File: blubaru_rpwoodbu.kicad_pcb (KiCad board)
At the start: 2 copper layers, 97.8 x 94.6 mm, 38 parts, among them J1 DB15, J2 DB15, J3 FSA2269, J4 ProMicro, J5 RN52_BREAKOUT, J6 JACK_TRS_6PINS, J7 TPA6112, P1 CONN_01X06, U1 DG419

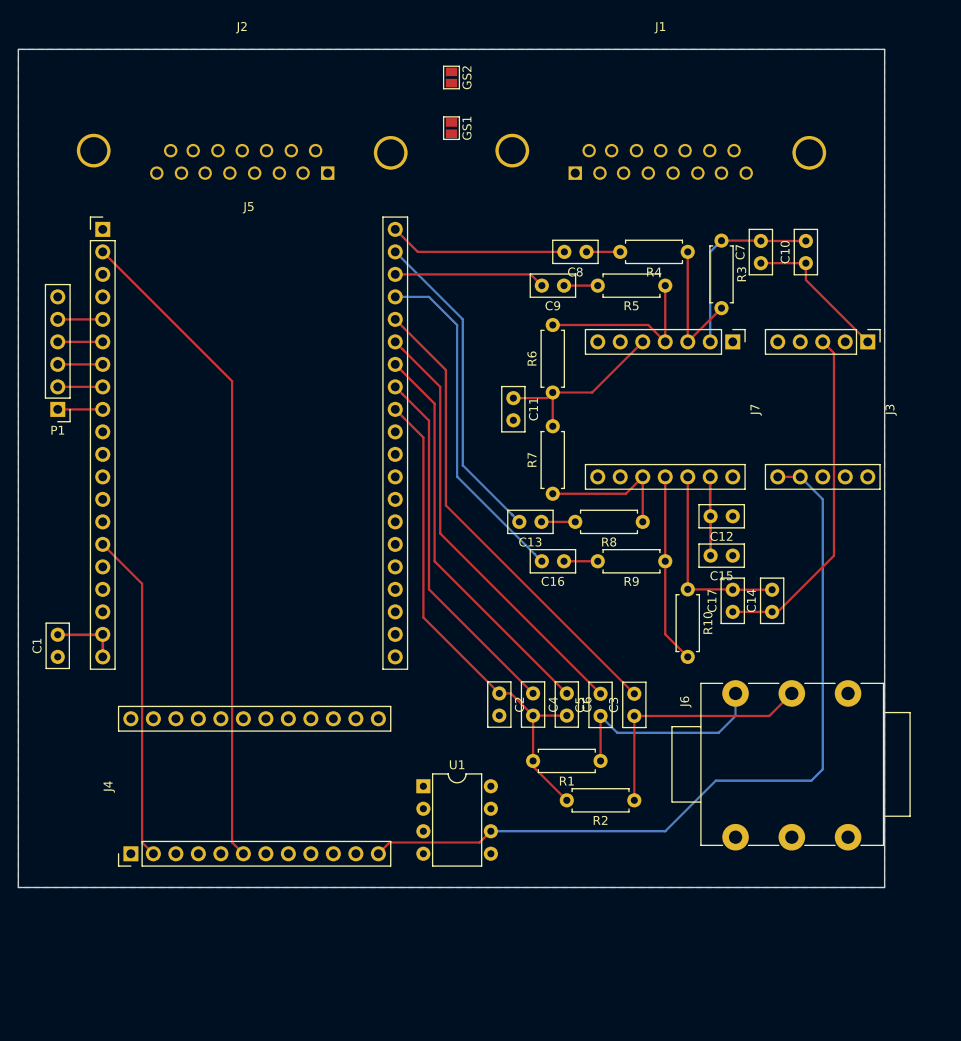
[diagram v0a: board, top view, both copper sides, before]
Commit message: jbebels attempt at routing
All power and audio is routed, as is the crystal and UART lines. Other
digital lines remain, and the resistors for the LEDs are moved off-board
until I figure out the best place for them.

This also required a small fix to the schematic. A junction was missing,
causing the audio grounds to not be connected to the cd/stereo audio
ground.
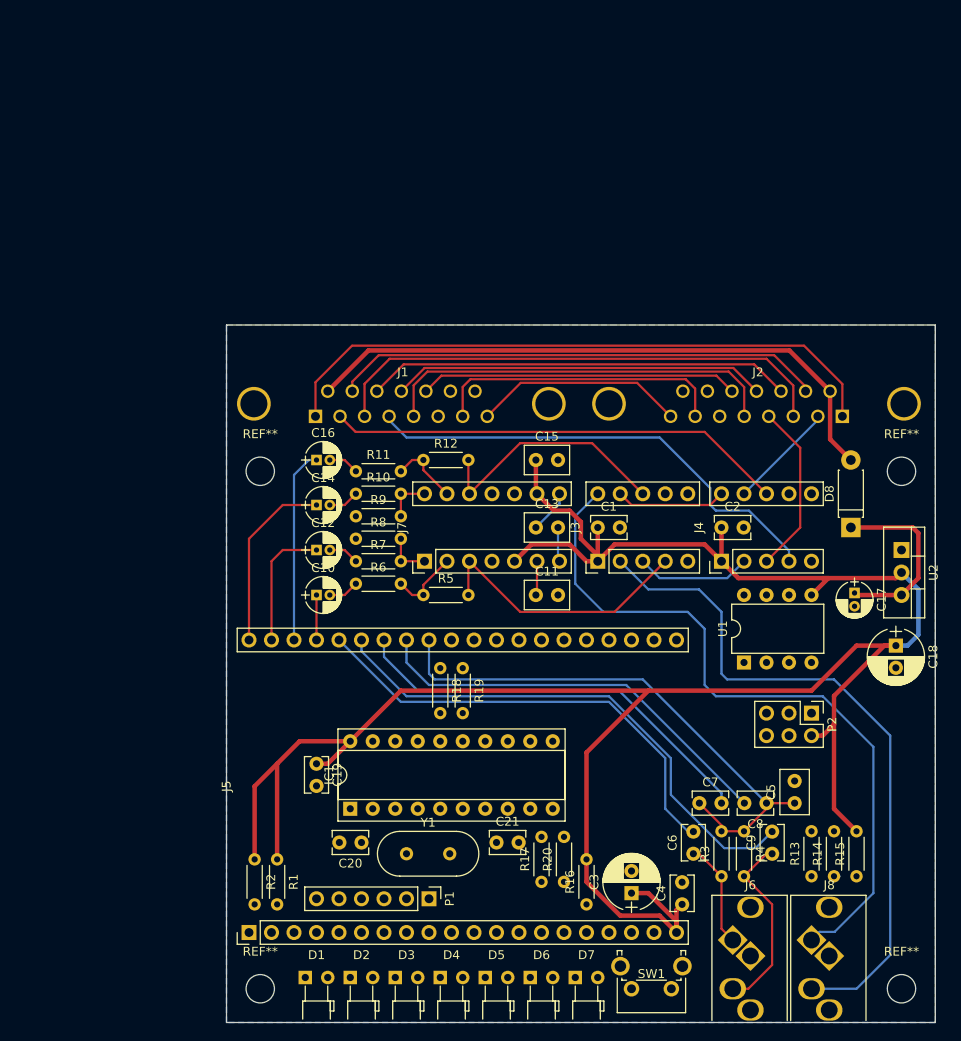
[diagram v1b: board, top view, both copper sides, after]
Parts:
- removed GS1, GS2: GS2, Connectors:GS2
- added C18: 100uF, blubaru:CP_Radial_D6.3mm_P2.50mm, F.Cu at (183.5, 97.2)
- added C19: 0.1uF, blubaru:C_Disc_D4.0mm_W2.6mm_P2.50mm, F.Cu at (118.1, 110.5)
- added C20: 22pF, blubaru:C_Disc_D4.0mm_W2.6mm_P2.50mm, F.Cu at (123.2, 119.4)
- added C21: 22pF, blubaru:C_Disc_D4.0mm_W2.6mm_P2.50mm, F.Cu at (138.4, 119.4)
- added D1: R LED, blubaru:LED_D3.0mm_Horizontal_O1.27mm_Z6.0mm, F.Cu at (116.8, 134.6)
- added D2: B LED, blubaru:LED_D3.0mm_Horizontal_O1.27mm_Z6.0mm, F.Cu at (121.9, 134.6)
- added D3: Y LED, blubaru:LED_D3.0mm_Horizontal_O1.27mm_Z6.0mm, F.Cu at (127.0, 134.6)
- added D4: O LED, blubaru:LED_D3.0mm_Horizontal_O1.27mm_Z6.0mm, F.Cu at (132.1, 134.6)
- added D5: G LED, blubaru:LED_D3.0mm_Horizontal_O1.27mm_Z6.0mm, F.Cu at (137.2, 134.6)
- added D6: B LED, blubaru:LED_D3.0mm_Horizontal_O1.27mm_Z6.0mm, F.Cu at (142.2, 134.6)
- added D7: R LED, blubaru:LED_D3.0mm_Horizontal_O1.27mm_Z6.0mm, F.Cu at (147.3, 134.6)
- added D8: D, Diodes_THT:D_DO-41_SOD81_P7.62mm_Horizontal, F.Cu at (178.4, 83.8)
- added IC1: ATTINY4313-P, blubaru:DIP-20_W7.62mm_Socket, F.Cu at (121.9, 115.6)
- added J8: JACK_TRS_5PINS, blubaru:sj1-353xng, F.Cu at (176.0, 138.3)
- added P2: CONN_02X03, Pin_Headers:Pin_Header_Straight_2x03_Pitch2.54mm, F.Cu at (174.0, 104.8)
- added R11: 11k, Resistors_THT:R_Axial_DIN0204_L3.6mm_D1.6mm_P5.08mm_Horizontal, F.Cu at (122.6, 77.5)
- added R12: 8.2k, Resistors_THT:R_Axial_DIN0204_L3.6mm_D1.6mm_P5.08mm_Horizontal, F.Cu at (130.2, 76.2)
- added R13: 100k, Resistors_THT:R_Axial_DIN0204_L3.6mm_D1.6mm_P5.08mm_Horizontal, F.Cu at (174.0, 123.2)
- added R14: 100k, Resistors_THT:R_Axial_DIN0204_L3.6mm_D1.6mm_P5.08mm_Horizontal, F.Cu at (176.5, 123.2)
- added R15: 1M, Resistors_THT:R_Axial_DIN0204_L3.6mm_D1.6mm_P5.08mm_Horizontal, F.Cu at (179.1, 123.2)
- added R16: 750, Resistors_THT:R_Axial_DIN0204_L3.6mm_D1.6mm_P5.08mm_Horizontal, F.Cu at (148.6, 126.4)
- added R17: 330, Resistors_THT:R_Axial_DIN0204_L3.6mm_D1.6mm_P5.08mm_Horizontal, F.Cu at (143.5, 123.8)
- added R18: 750, Resistors_THT:R_Axial_DIN0204_L3.6mm_D1.6mm_P5.08mm_Horizontal, F.Cu at (132.1, 99.7)
- added R19: 750, Resistors_THT:R_Axial_DIN0204_L3.6mm_D1.6mm_P5.08mm_Horizontal, F.Cu at (134.6, 99.7)
- added R20: 330, Resistors_THT:R_Axial_DIN0204_L3.6mm_D1.6mm_P5.08mm_Horizontal, F.Cu at (146.1, 123.8)
- added REF**: MountingHole_3.2mm_M3, Mounting_Holes:MountingHole_3.2mm_M3, F.Cu at (184.2, 135.9)
- added REF**: MountingHole_3.2mm_M3, Mounting_Holes:MountingHole_3.2mm_M3, F.Cu at (111.8, 135.9)
- added REF**: MountingHole_3.2mm_M3, Mounting_Holes:MountingHole_3.2mm_M3, F.Cu at (184.2, 77.5)
- added REF**: MountingHole_3.2mm_M3, Mounting_Holes:MountingHole_3.2mm_M3, F.Cu at (111.8, 77.5)
- added SW1: SW_Push, blubaru:SW_Tactile_SPST_Angled_PTS645Vx58-2LFS, F.Cu at (158.2, 135.9)
- added U2: LD1117V33, TO_SOT_Packages_THT:TO-220_Vertical, F.Cu at (184.2, 86.4)
- added Y1: 11.0592MHz, Crystals:Crystal_HC49-4H_Vertical, F.Cu at (128.3, 120.7)
- C1: footprint Capacitors_THT:C_Disc_D5.0mm_W2.5mm_P2.50mm -> blubaru:C_Disc_D4.0mm_W2.6mm_P2.50mm
- C10, C14: value 100uF -> 1uF; footprint Capacitors_THT:C_Disc_D5.0mm_W2.5mm_P2.50mm -> blubaru:CP_Radial_D4.0mm_P1.50mm
- C11, C13: footprint Capacitors_THT:C_Disc_D5.0mm_W2.5mm_P2.50mm -> blubaru:C_Disc_D5.0mm_W3.2mm_P2.50mm
- C12: value 0.1uF -> 1uF; footprint Capacitors_THT:C_Disc_D5.0mm_W2.5mm_P2.50mm -> blubaru:CP_Radial_D4.0mm_P1.50mm
- C15: value 10uF -> 1uF; footprint Capacitors_THT:C_Disc_D5.0mm_W2.5mm_P2.50mm -> blubaru:C_Disc_D5.0mm_W3.2mm_P2.50mm
- C16: footprint Capacitors_THT:C_Disc_D5.0mm_W2.5mm_P2.50mm -> blubaru:CP_Radial_D4.0mm_P1.50mm
- C17: value 100uF -> 10uF; footprint Capacitors_THT:C_Disc_D5.0mm_W2.5mm_P2.50mm -> blubaru:CP_Radial_D4.0mm_P1.50mm
- C2: value 1uF -> 0.1uF; footprint Capacitors_THT:C_Disc_D5.0mm_W2.5mm_P2.50mm -> blubaru:C_Disc_D4.0mm_W2.6mm_P2.50mm
- C3: value 47nF -> 220uF; footprint Capacitors_THT:C_Disc_D5.0mm_W2.5mm_P2.50mm -> blubaru:CP_Radial_D6.3mm_P2.50mm
- C4: value 47nF -> 0.1uF; footprint Capacitors_THT:C_Disc_D5.0mm_W2.5mm_P2.50mm -> blubaru:C_Disc_D4.0mm_W2.6mm_P2.50mm
- C5: value 47nF -> 1uF; footprint Capacitors_THT:C_Disc_D5.0mm_W2.5mm_P2.50mm -> blubaru:C_Disc_D5.0mm_W3.2mm_P2.50mm
- C6: value 47nF -> 0.047uF; footprint Capacitors_THT:C_Disc_D5.0mm_W2.5mm_P2.50mm -> blubaru:C_Disc_D4.0mm_W2.6mm_P2.50mm
- C7: value 100uF -> 0.047uF; footprint Capacitors_THT:C_Disc_D5.0mm_W2.5mm_P2.50mm -> blubaru:C_Disc_D4.0mm_W2.6mm_P2.50mm
- C8, C9: value 1uF -> 0.047uF; footprint Capacitors_THT:C_Disc_D5.0mm_W2.5mm_P2.50mm -> blubaru:C_Disc_D4.0mm_W2.6mm_P2.50mm
- J1: footprint Connectors:DB15FC -> blubaru:DB15FC
- J2: footprint Connectors:DB15MC -> blubaru:DB15MC
- J3: value FSA2269 -> TS5A22364-Q1; footprint blubaru:FSA2269 -> blubaru:TS5A22364-Q1
- J4: value ProMicro -> TS5A22364-Q1; footprint blubaru:ProMicro -> blubaru:TS5A22364-Q1
- J6: value JACK_TRS_6PINS -> JACK_TRS_5PINS; footprint Connectors:NMJ6HCD2 -> blubaru:sj1-353xng
- J7: value TPA6112 -> DRV632; footprint blubaru:TPA6112 -> blubaru:DRV632
- R1: value 2k2 -> 330; footprint Resistors_THT:R_Axial_DIN0207_L6.3mm_D2.5mm_P7.62mm_Horizontal -> Resistors_THT:R_Axial_DIN0204_L3.6mm_D1.6mm_P5.08mm_Horizontal
- R10, R6, R7: value 47k -> 11k; footprint Resistors_THT:R_Axial_DIN0207_L6.3mm_D2.5mm_P7.62mm_Horizontal -> Resistors_THT:R_Axial_DIN0204_L3.6mm_D1.6mm_P5.08mm_Horizontal
- R2: value 2k2 -> 750; footprint Resistors_THT:R_Axial_DIN0207_L6.3mm_D2.5mm_P7.62mm_Horizontal -> Resistors_THT:R_Axial_DIN0204_L3.6mm_D1.6mm_P5.08mm_Horizontal
- R3: value 47k -> 2k2; footprint Resistors_THT:R_Axial_DIN0207_L6.3mm_D2.5mm_P7.62mm_Horizontal -> Resistors_THT:R_Axial_DIN0204_L3.6mm_D1.6mm_P5.08mm_Horizontal
- R4: value 22k -> 2k2; footprint Resistors_THT:R_Axial_DIN0207_L6.3mm_D2.5mm_P7.62mm_Horizontal -> Resistors_THT:R_Axial_DIN0204_L3.6mm_D1.6mm_P5.08mm_Horizontal
- R5, R8, R9: value 22k -> 8.2k; footprint Resistors_THT:R_Axial_DIN0207_L6.3mm_D2.5mm_P7.62mm_Horizontal -> Resistors_THT:R_Axial_DIN0204_L3.6mm_D1.6mm_P5.08mm_Horizontal
- moved J4 72.8 mm to (163.8, 83.8)
- moved R3 71.8 mm to (163.8, 123.2), turned to 90 degrees
- moved P1 69.3 mm to (130.8, 125.7), turned to 270 degrees
- moved C9 68.3 mm to (169.5, 120.7), turned to 90 degrees
- moved C10 66.8 mm to (118.1, 91.4), turned to 0 degrees
- moved R4 65.7 mm to (166.4, 118.1), turned to 270 degrees
- moved C8 65.5 mm to (168.9, 114.9)
- moved J2 64.3 mm to (177.5, 71.3)
- moved J5 62.9 mm to (110.5, 113.0), turned to 90 degrees
- moved C1 62.7 mm to (149.9, 83.8), turned to 0 degrees
- moved C7 61.4 mm to (161.3, 114.9), turned to 0 degrees
- moved C14 52.8 mm to (118.1, 81.3), turned to 0 degrees
- moved C12 47.1 mm to (118.1, 86.4), turned to 0 degrees
- moved R5 44.3 mm to (130.2, 91.4), turned to 0 degrees
- moved R2 43.4 mm to (111.1, 121.3), turned to 270 degrees
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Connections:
- C1 pad 1: GND -> VCC
- C1 pad 2: VCC -> GND
- C10 pad 1: /DB-15 interconnects/Modules/Audio switch/BT_L -> /DB-15 interconnects/Modules/Bluetooth Module/Line Driver/R-
- C12 pad 1: GND -> /DB-15 interconnects/Modules/Bluetooth Module/Line Driver/R+
- C12 pad 2: VCC -> Net-(C12-Pad2)
- C13 pad 2: /DB-15 interconnects/Modules/Bluetooth Module/Amp/R+ -> Net-(C13-Pad2)
- C14 pad 1: /DB-15 interconnects/Modules/Audio switch/BT_R -> /DB-15 interconnects/Modules/Bluetooth Module/Line Driver/L+
- C15 pad 1: GND -> VCC
- C15 pad 2: VCC -> GND
- C16 pad 1: Net-(C16-Pad1) -> /DB-15 interconnects/Modules/Bluetooth Module/Line Driver/L-
- C16 pad 2: /DB-15 interconnects/Modules/Bluetooth Module/Amp/R- -> Net-(C16-Pad2)
- C17 pad 1: /DB-15 interconnects/Modules/Audio switch/BT_R -> +12V
- C17 pad 2: Net-(C14-Pad2) -> GND
- C2 pad 1: /DB-15 interconnects/Modules/Bluetooth Module/Microphone/MIC_BIAS -> VCC
- C3 pad 1: Net-(C3-Pad1) -> VCC
- C3 pad 2: /DB-15 interconnects/Modules/Bluetooth Module/Microphone/MIC_R- -> GND
- C4 pad 1: /DB-15 interconnects/Modules/Bluetooth Module/Microphone/MIC_L+ -> VCC
- C4 pad 2: /DB-15 interconnects/Modules/Bluetooth Module/Microphone/MIC_BIAS -> GND
- C5 pad 1: Net-(C5-Pad1) -> /DB-15 interconnects/Modules/Bluetooth Module/Microphone/MIC_BIAS
- C5 pad 2: /DB-15 interconnects/Modules/Bluetooth Module/Microphone/MIC_L- -> GND
- C6 pad 1: /DB-15 interconnects/Modules/Bluetooth Module/Microphone/MIC_R+ -> Net-(C6-Pad1)
- C6 pad 2: /DB-15 interconnects/Modules/Bluetooth Module/Microphone/MIC_BIAS -> /DB-15 interconnects/Modules/Bluetooth Module/Microphone/MIC_R-
- C7 pad 1: /DB-15 interconnects/Modules/Audio switch/BT_L -> /DB-15 interconnects/Modules/Bluetooth Module/Microphone/MIC_BIAS
- C7 pad 2: Net-(C10-Pad2) -> /DB-15 interconnects/Modules/Bluetooth Module/Microphone/MIC_R+
- C8 pad 1: Net-(C8-Pad1) -> /DB-15 interconnects/Modules/Bluetooth Module/Microphone/MIC_BIAS
- C8 pad 2: /DB-15 interconnects/Modules/Bluetooth Module/Amp/L+ -> /DB-15 interconnects/Modules/Bluetooth Module/Microphone/MIC_L+
- C9 pad 2: /DB-15 interconnects/Modules/Bluetooth Module/Amp/L- -> /DB-15 interconnects/Modules/Bluetooth Module/Microphone/MIC_L-
- J1 pad 15: (no net) -> Net-(J1-Pad15)
- J1 pad 5: /DB-15 interconnects/5_IN -> GNDA
- J1 pad 9: +12V -> +BATT
- J2 pad 15: (no net) -> Net-(J2-Pad15)
- J2 pad 5: /DB-15 interconnects/5_IN -> GNDA
- J2 pad 9: +12V -> +BATT
- J3 pad 1: /DB-15 interconnects/Modules/Audio switch/BT_L -> VCC
- J3 pad 10: /DB-15 interconnects/4_IN -> /DB-15 interconnects/Modules/Audio switch/LINE_R
- J3 pad 2: /DB-15 interconnects/2_IN -> /DB-15 interconnects/Modules/Audio switch/LINE_L
- J3 pad 3: /DB-15 interconnects/Modules/Audio switch/BT_R -> Net-(J3-Pad3)
- J3 pad 4: GND -> /DB-15 interconnects/Modules/Audio switch/BT_L
- J3 pad 5: /DB-15 interconnects/2_OUT -> /DB-15 interconnects/Modules/Audio switch/LINE_TRG
- J3 pad 6: /DB-15 interconnects/Modules/Audio switch/BT_TRG -> GND
- J3 pad 7: /DB-15 interconnects/Modules/Audio switch/BT_TRG -> /DB-15 interconnects/Modules/Audio switch/LINE_TRG
- J3 pad 8: /DB-15 interconnects/4_OUT -> /DB-15 interconnects/Modules/Audio switch/BT_R
- J3 pad 9: VCC -> Net-(J3-Pad9)
- J4 pad 1: /DB-15 interconnects/Modules/Bluetooth Module/UART_RX -> VCC
- J4 pad 10: (no net) -> Net-(J3-Pad9)
- J4 pad 2: /DB-15 interconnects/Modules/Bluetooth Module/UART_TX -> Net-(J3-Pad3)
- J4 pad 3: GND -> /DB-15 interconnects/4_OUT
- J4 pad 4: GND -> /DB-15 interconnects/4_IN
- J4 pad 5: /DB-15 interconnects/Modules/Bluetooth Module/CMD -> /DB-15 interconnects/Modules/Audio switch/BT_TRG
- J4 pad 6: /DB-15 interconnects/Modules/Bluetooth Module/EVENT -> GND
- J4 pad 7: (no net) -> /DB-15 interconnects/Modules/Audio switch/BT_TRG
- J4 pad 8: (no net) -> /DB-15 interconnects/2_IN
- J4 pad 9: (no net) -> /DB-15 interconnects/2_OUT
- J5 pad 1: (no net) -> /DB-15 interconnects/Modules/Microcontroller/BT_RESET
- J5 pad 11: (no net) -> Net-(J5-Pad11)
- J5 pad 12: (no net) -> Net-(J5-Pad12)
- J5 pad 13: (no net) -> Net-(J5-Pad13)
- J5 pad 14: (no net) -> Net-(J5-Pad14)
- J5 pad 17: (no net) -> /DB-15 interconnects/Modules/Bluetooth Module/9600
- J5 pad 18: (no net) -> Net-(J5-Pad18)
- J5 pad 19: VCC -> /DB-15 interconnects/Modules/Bluetooth Module/PWR_EN
- J5 pad 22: (no net) -> Net-(J5-Pad22)
- J5 pad 23: (no net) -> Net-(J5-Pad23)
- J5 pad 24: (no net) -> Net-(J5-Pad24)
- J5 pad 25: (no net) -> Net-(J5-Pad25)
- J5 pad 26: (no net) -> Net-(J5-Pad26)
- J5 pad 27: (no net) -> Net-(J5-Pad27)
- J5 pad 28: (no net) -> Net-(J5-Pad28)
- J5 pad 29: (no net) -> Net-(J5-Pad29)
- J5 pad 3: (no net) -> Net-(J5-Pad3)
- J5 pad 30: (no net) -> Net-(D7-Pad1)
- J5 pad 31: (no net) -> Net-(D6-Pad1)
- J5 pad 37: /DB-15 interconnects/Modules/Bluetooth Module/Amp/R- -> /DB-15 interconnects/Modules/Bluetooth Module/Line Driver/R-
- J5 pad 38: /DB-15 interconnects/Modules/Bluetooth Module/Amp/L- -> /DB-15 interconnects/Modules/Bluetooth Module/Line Driver/L-
- J5 pad 39: /DB-15 interconnects/Modules/Bluetooth Module/Amp/R+ -> /DB-15 interconnects/Modules/Bluetooth Module/Line Driver/R+
- J5 pad 4: (no net) -> Net-(J5-Pad4)
- J5 pad 40: /DB-15 interconnects/Modules/Bluetooth Module/Amp/L+ -> /DB-15 interconnects/Modules/Bluetooth Module/Line Driver/L+
- J6 pad 2: Net-(C5-Pad1) -> Net-(C9-Pad1)
- J6 pad 3: Net-(C3-Pad1) -> Net-(C6-Pad1)
- J6 pad 4: (no net) -> Net-(J6-Pad4)
- J6 pad 5: (no net) -> Net-(J6-Pad5)
- J7 pad 1: GND -> Net-(J7-Pad1)
- J7 pad 10: Net-(J7-Pad10) -> GND
- J7 pad 12: Net-(C14-Pad2) -> /DB-15 interconnects/Modules/Audio switch/BT_R
- J7 pad 13: VCC -> Net-(J7-Pad13)
- J7 pad 14: GND -> Net-(J7-Pad14)
- J7 pad 2: Net-(C10-Pad2) -> Net-(J7-Pad2)
- J7 pad 3: Net-(J7-Pad3) -> /DB-15 interconnects/Modules/Audio switch/BT_L
- J7 pad 4: Net-(J7-Pad4) -> GND
- J7 pad 5: Net-(C11-Pad1) -> VCC
- J7 pad 6: GND -> Net-(C11-Pad1)
- J7 pad 7: GND -> Net-(C13-Pad2)
- J7 pad 8: GND -> Net-(C13-Pad1)
- J7 pad 9: GND -> VCC
- R1 pad 1: Net-(C5-Pad1) -> VCC
- R1 pad 2: /DB-15 interconnects/Modules/Bluetooth Module/Microphone/MIC_BIAS -> Net-(D6-Pad2)
- R10 pad 2: Net-(J7-Pad11) -> Net-(J7-Pad14)
- R2 pad 1: Net-(C3-Pad1) -> VCC
- R2 pad 2: /DB-15 interconnects/Modules/Bluetooth Module/Microphone/MIC_BIAS -> Net-(D7-Pad2)
- R3 pad 1: Net-(C10-Pad2) -> Net-(C6-Pad1)
- R3 pad 2: Net-(J7-Pad3) -> /DB-15 interconnects/Modules/Bluetooth Module/Microphone/MIC_BIAS
- R4 pad 1: Net-(J7-Pad3) -> /DB-15 interconnects/Modules/Bluetooth Module/Microphone/MIC_BIAS
- R4 pad 2: Net-(C8-Pad1) -> Net-(C9-Pad1)
- R5 pad 1: Net-(J7-Pad4) -> Net-(J7-Pad2)
- R5 pad 2: Net-(C9-Pad1) -> /DB-15 interconnects/Modules/Audio switch/BT_L
- R6 pad 1: Net-(C11-Pad1) -> Net-(C10-Pad2)
- R6 pad 2: Net-(J7-Pad4) -> Net-(J7-Pad2)
- R7 pad 1: Net-(J7-Pad10) -> Net-(C12-Pad2)
- R7 pad 2: Net-(C11-Pad1) -> Net-(J7-Pad1)
- R8 pad 1: Net-(J7-Pad10) -> GNDA
- R8 pad 2: Net-(C13-Pad1) -> Net-(J7-Pad1)
- R9 pad 1: Net-(J7-Pad11) -> GNDA
- R9 pad 2: Net-(C16-Pad1) -> Net-(J7-Pad14)
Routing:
- net VCC: track 16.6 -> 264.8 mm
- net /DB-15 interconnects/Modules/Audio switch/BT_TRG: track 90.7 -> 0.00 mm
- net /DB-15 interconnects/Modules/Audio switch/LINE_R: track 0.00 -> 81.9 mm
- net /DB-15 interconnects/Modules/Audio switch/LINE_L: track 0.00 -> 78.6 mm
- net /DB-15 interconnects/Modules/Bluetooth Module/EVENT: track 74.5 -> 0.00 mm
- net /DB-15 interconnects/1_IN: track 0.00 -> 70.5 mm
- net +BATT: track 0.00 -> 69.3 mm
- net /DB-15 interconnects/3_IN: track 0.38 -> 58.0 mm
- net /DB-15 interconnects/10_IN: track 0.30 -> 55.5 mm
- net /DB-15 interconnects/4_IN: track 0.00 -> 54.0 mm
- net /DB-15 interconnects/2_IN: track 0.00 -> 51.8 mm
- net /DB-15 interconnects/11_IN: track 0.07 -> 48.1 mm
- net GNDA: track 0.00 -> 45.5 mm
- net /DB-15 interconnects/12_IN: track 0.12 -> 42.3 mm
- net /DB-15 interconnects/Modules/Bluetooth Module/Amp/R-: track 38.9 -> 0.00 mm
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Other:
- board size 97.8 x 94.6 mm -> 80 x 78.7 mm
- net class Power: trace_width 0.3048 -> 0.508
